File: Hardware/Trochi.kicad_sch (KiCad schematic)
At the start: 37 parts, among them IC1 ICM-42688-P, J1 JST PH, J2 JST-SH, J3 JST-SH, J4 JST-SH, J5 JST-SH, J6 JST_SH, Q1 AO3400A, Q2 AO3400A, Q3 AO3400A, Q4 AO3400A, SW1 SW_SPDT, U1 ME6211C33M5

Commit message: feat: add 3.3V regulator status LED to schematic
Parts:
- added D5: LED_RED, symbol Device:LED_Small_Filled
- added R4: 1K, symbol Device:R_Small_US
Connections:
- net +3.3V: now also D5.2 (A)
- net GND: now also R4.2
- new net: D5.1 (K), R4.1
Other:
- moved on the sheet: D1, D2, D3, D4, J2, J3, J4, J5, J6, Q1, Q2, Q3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

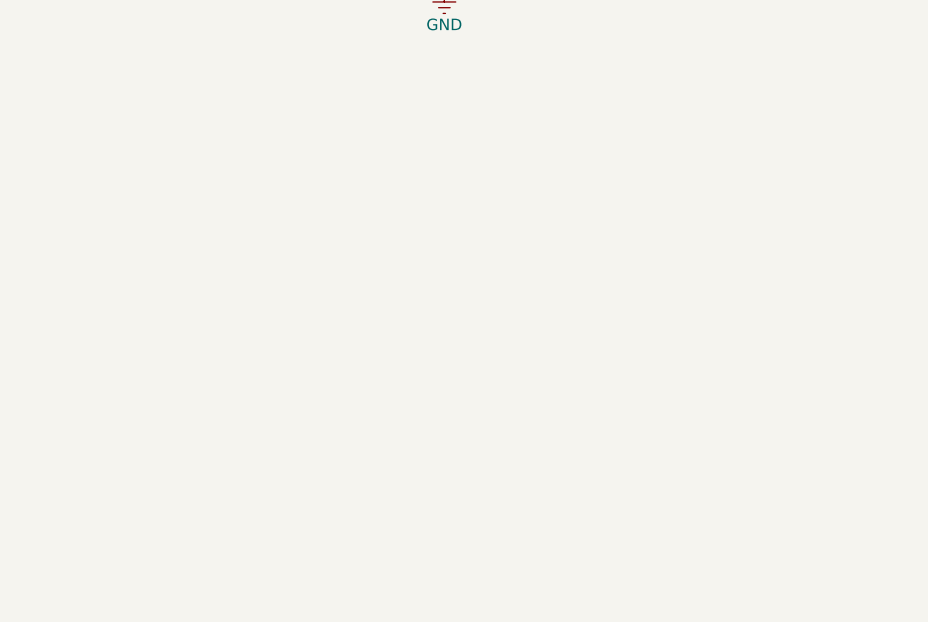
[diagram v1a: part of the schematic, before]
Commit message: feat: add buzzer circuit to schematic
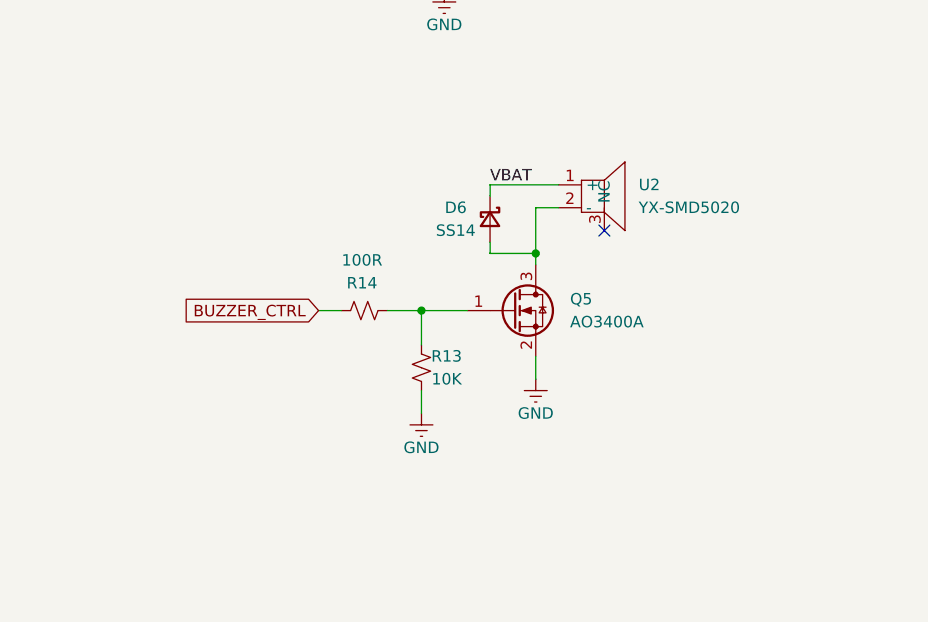
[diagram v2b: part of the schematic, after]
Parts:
- added D6: SS14, symbol Device:D_Schottky_Small
- added Q5: AO3400A, Package_TO_SOT_SMD:SOT-23, symbol Transistor_FET:AO3400A
- added R13: 10K, symbol Device:R_Small_US
- added R14: 100R, symbol Device:R_Small_US
- added U2: YX-SMD5020, trochi_footprint:BUZ-SMD_3P_L5.0-W5.0-P3.50-TL, symbol trochi_sym:YX-SMD5020
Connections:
- net GND: now also Q5.2 (S), R13.2
- net VBAT: now also D6.1 (K), U2.1 (+)
- new net: Q5.1 (G), R13.1, R14.2
- new net: D6.2 (A), Q5.3 (D), U2.2 (-)
- new net BUZZER_CTRL: R14.1
- no-connect marks 4 -> 5

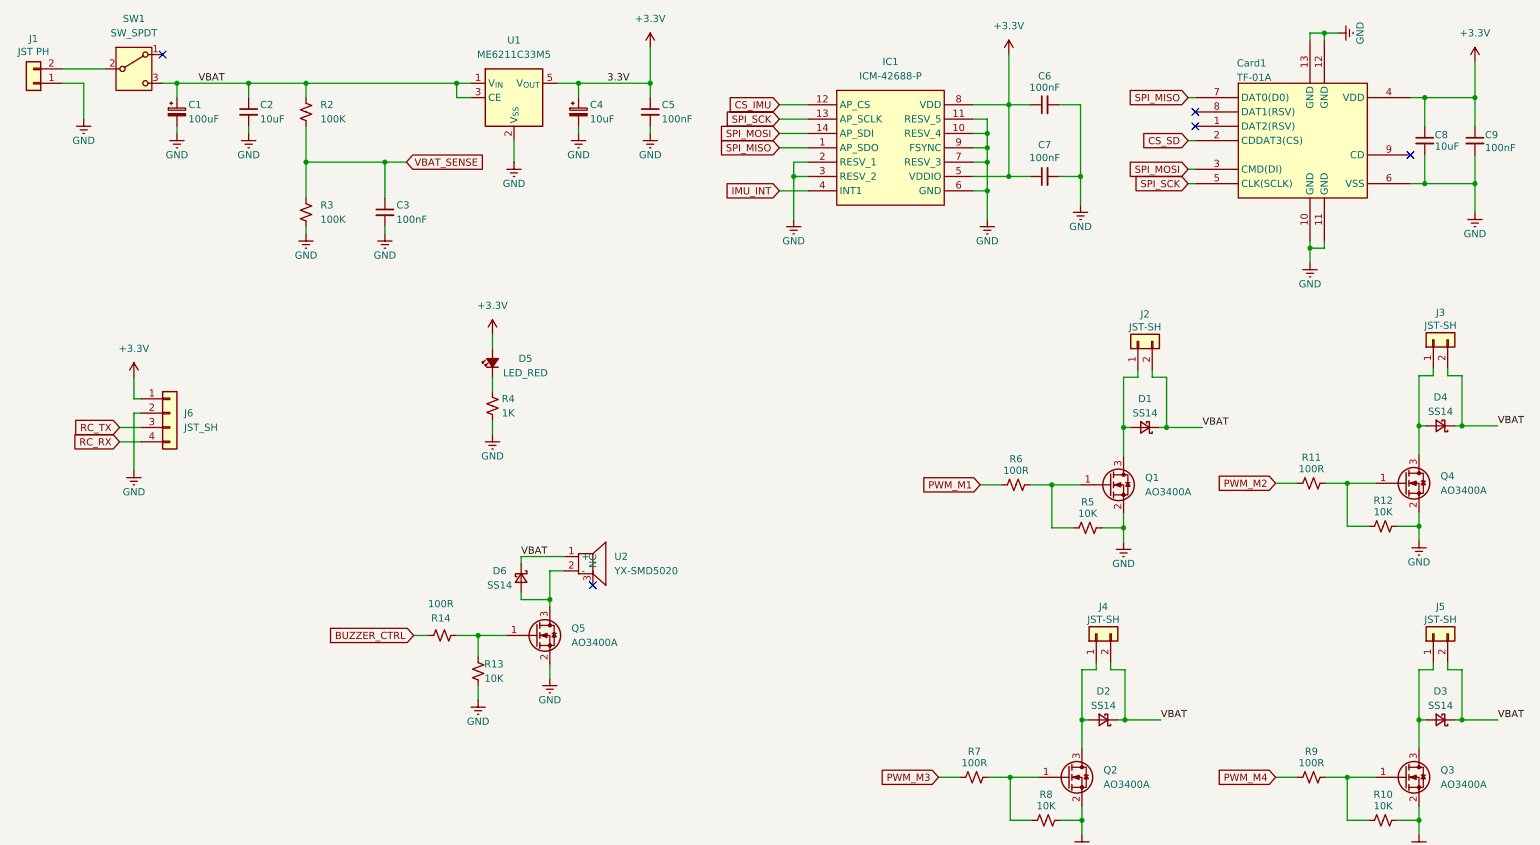
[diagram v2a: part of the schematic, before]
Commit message: feat: add pull-up resistors to SPI bus for IMU and SD card stability
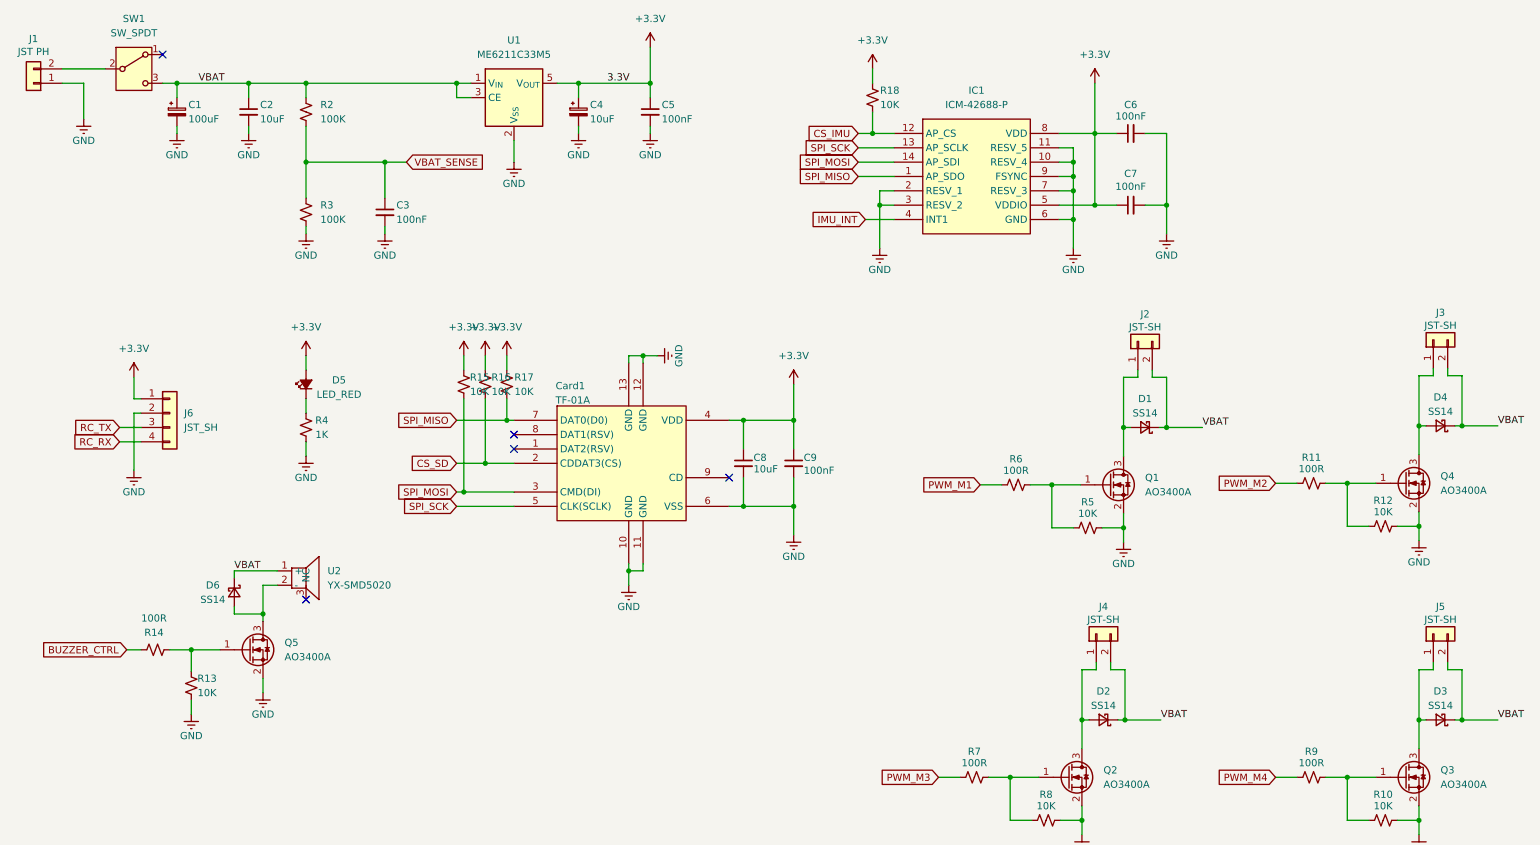
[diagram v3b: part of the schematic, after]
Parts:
- added R15, R16, R17, R18: 10K, symbol Device:R_Small_US
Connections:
- net +3.3V: now also R15.1, R16.1, R17.1, R18.1
- net CS_IMU: now also R18.2
- net CS_SD: now also R16.2
- net SPI_MISO: now also R17.2
- net SPI_MOSI: now also R15.2
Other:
- moved on the sheet: C6, C7, C8, C9, Card1, D5, D6, IC1, Q5, R13, R14, R4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

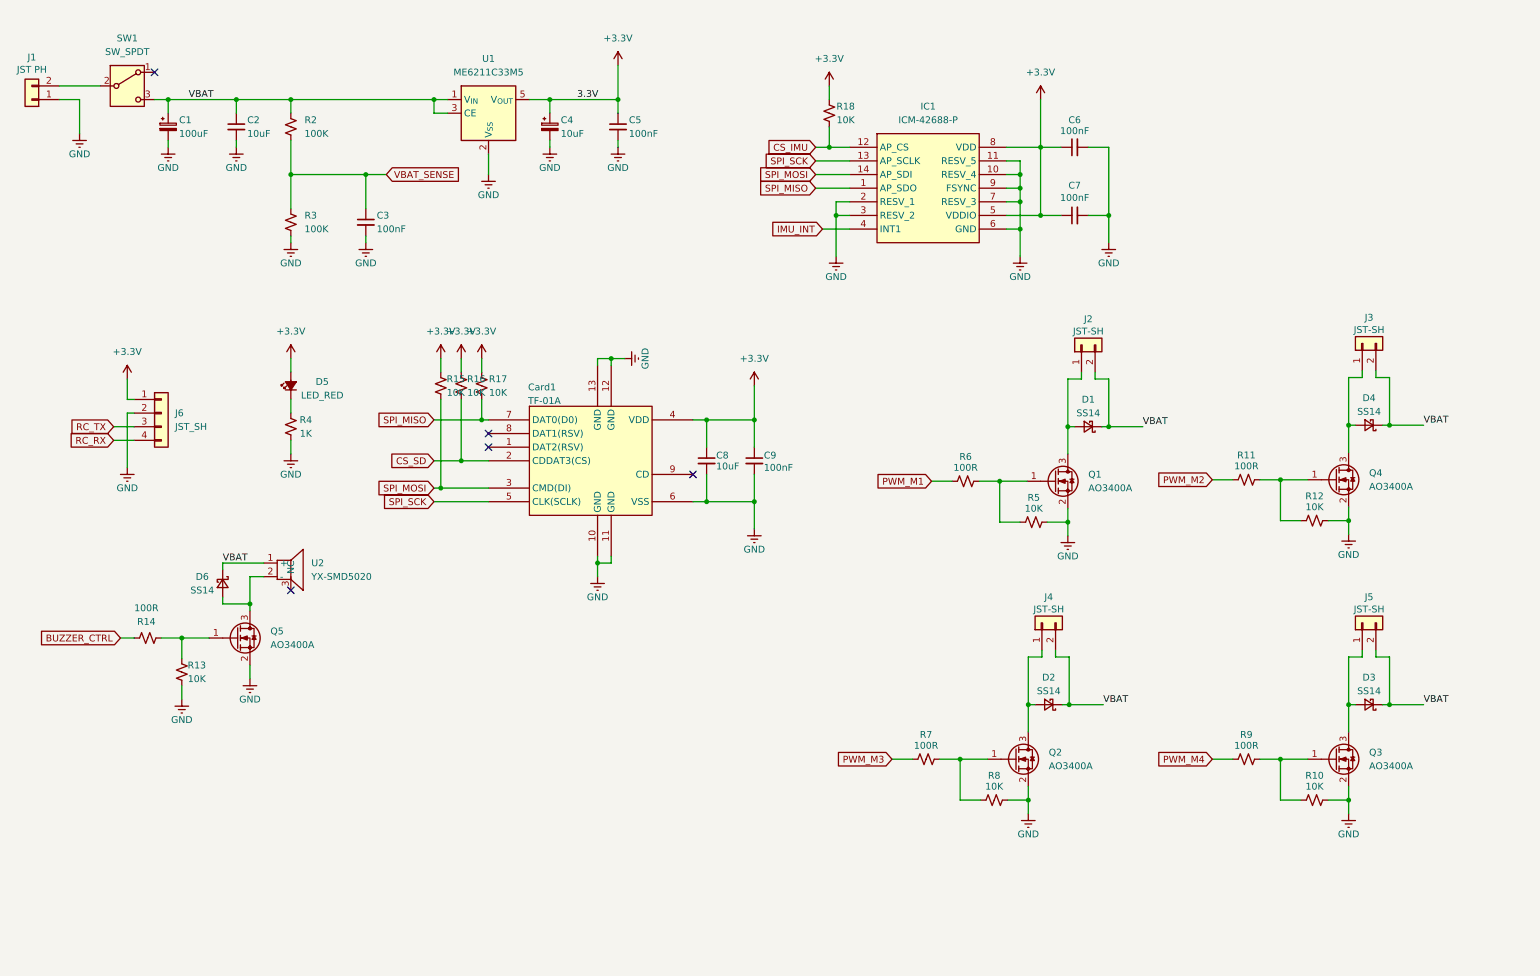
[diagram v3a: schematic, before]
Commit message: feat: add ESP32-S3 SuperMini to schematic with pin assignments
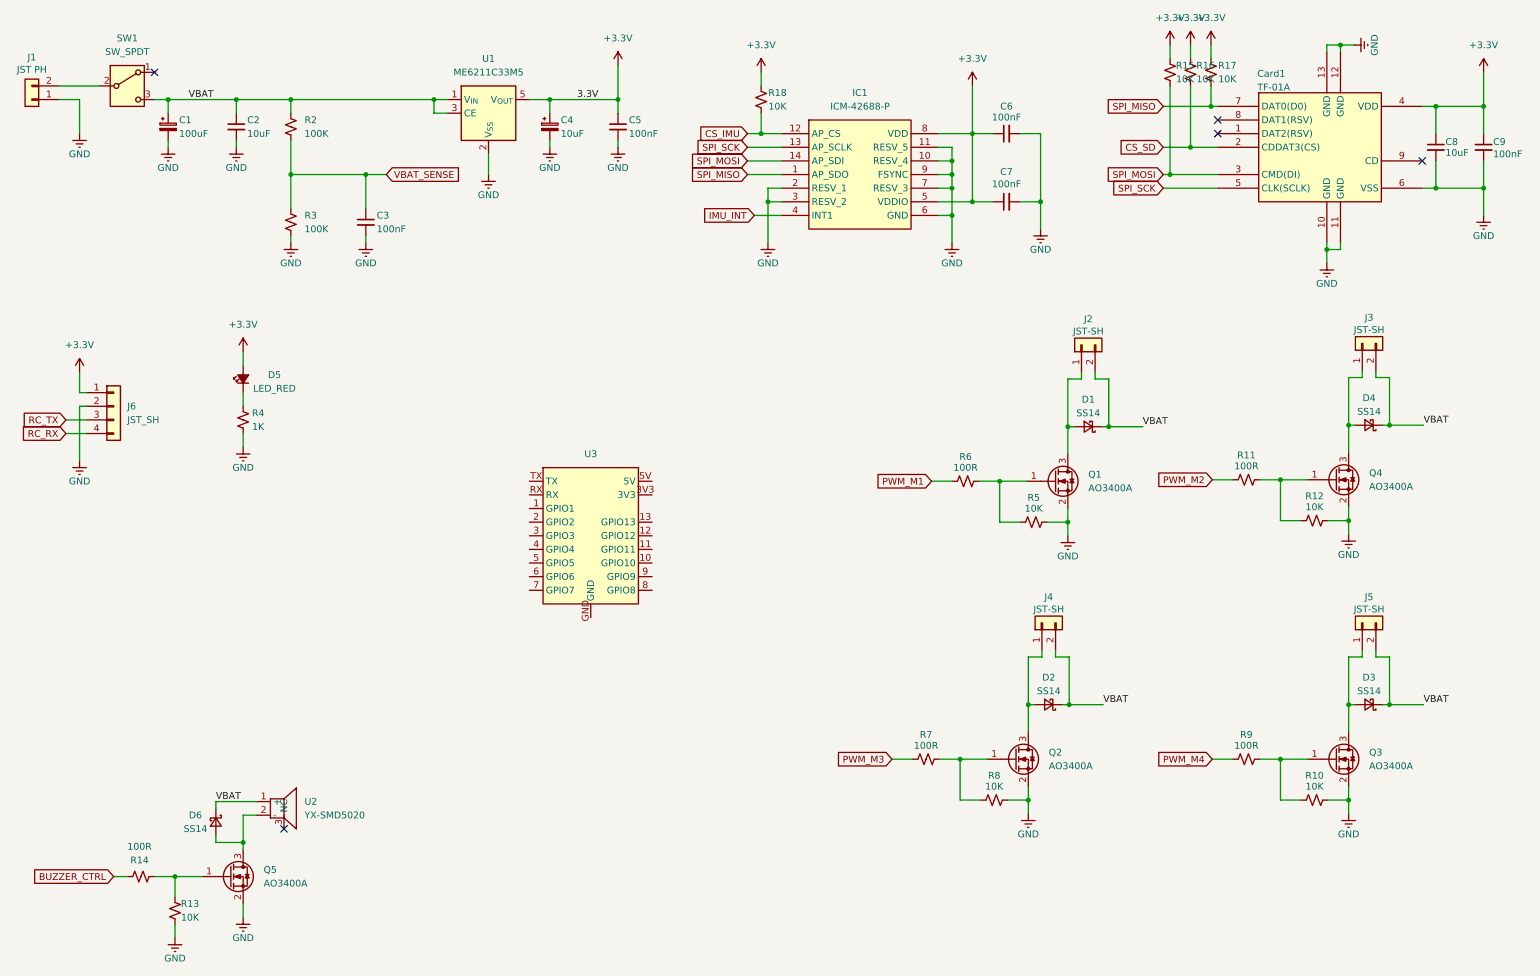
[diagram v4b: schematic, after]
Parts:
- added U3: (no value), trochi_footprint:esp32_s3_supermini, symbol trochi_sym:esp32_s3_supermini
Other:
- moved on the sheet: C6, C7, C8, C9, Card1, D5, D6, IC1, J6, Q5, R13, R14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

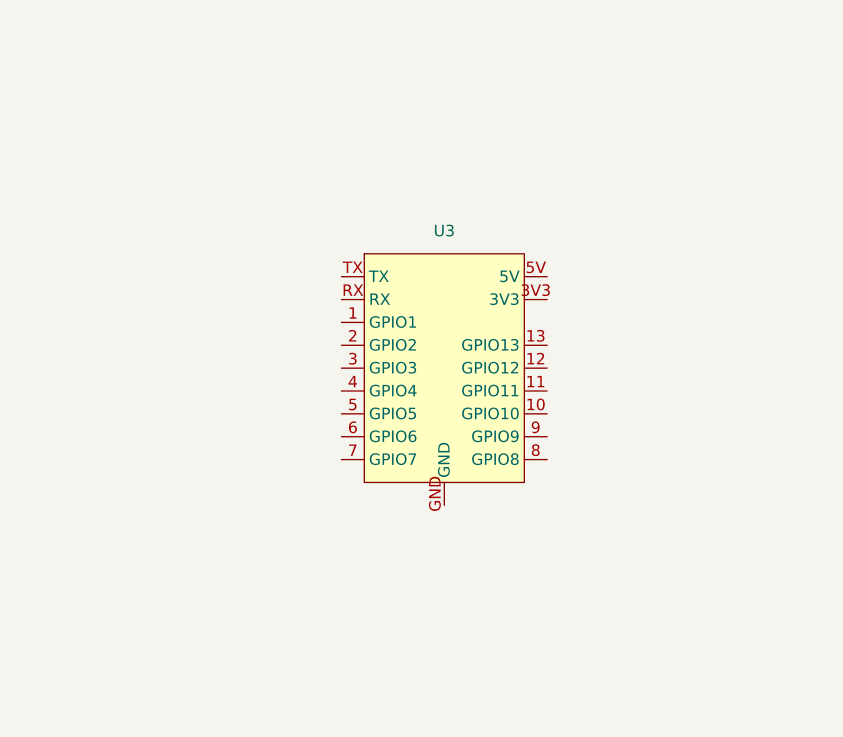
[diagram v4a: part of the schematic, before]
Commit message: feat: wire ESP32-S3 SuperMini header net connections
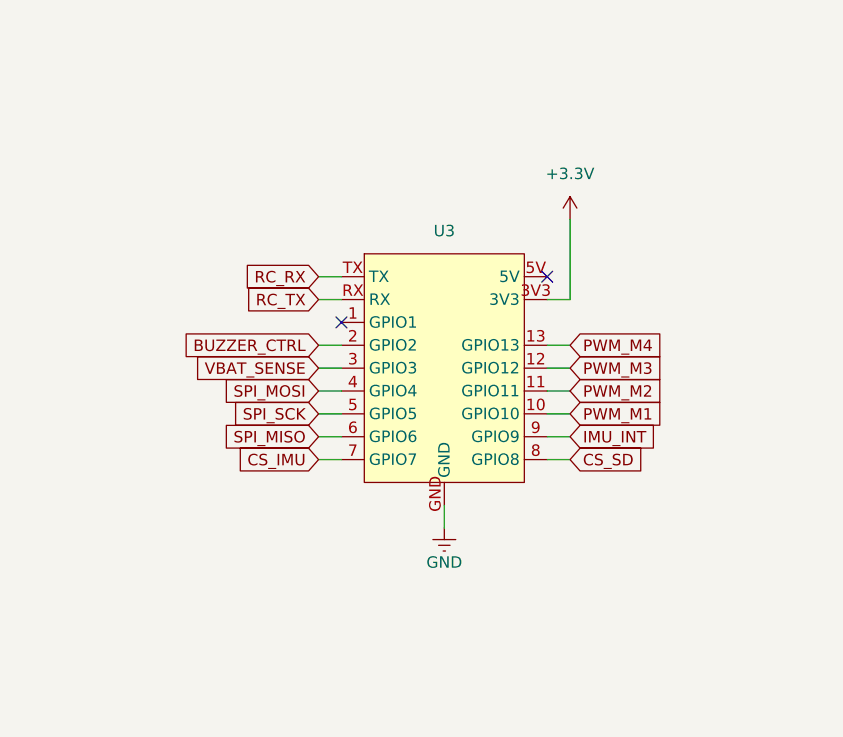
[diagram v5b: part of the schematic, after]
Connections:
- net +3.3V: now also U3.3V3
- net BUZZER_CTRL: now also U3.2 (GPIO2)
- net CS_IMU: now also U3.7 (GPIO7)
- net CS_SD: now also U3.8 (GPIO8)
- net GND: now also U3.GND
- net IMU_INT: now also U3.9 (GPIO9)
- net PWM_M1: now also U3.10 (GPIO10)
- net PWM_M2: now also U3.11 (GPIO11)
- net PWM_M3: now also U3.12 (GPIO12)
- net PWM_M4: now also U3.13 (GPIO13)
- net RC_RX: now also U3.TX
- net RC_TX: now also U3.RX
- net SPI_MISO: now also U3.6 (GPIO6)
- net SPI_MOSI: now also U3.4 (GPIO4)
- net SPI_SCK: now also U3.5 (GPIO5)
- net VBAT_SENSE: now also U3.3 (GPIO3)
- no-connect marks 5 -> 7

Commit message: style: organize and finalize schematic layout
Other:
- note added: "BUZZER"
- note added: "DRIVER'S"
- note added: "EXT"
- note added: "IMU"
- note added: "MCU"
- note added: "POWER"
- note added: "TF-CARD"
- moved on the sheet: C1, C2, C3, C4, C5, C6, C7, C8, C9, Card1, D1, D2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

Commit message: docs: specify schematic title block details
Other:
- company: (none) -> 2j87
- title: (none) -> Trochi
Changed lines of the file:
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@@
 	(generator_version "10.0")
 	(paper "A4")
+	(title_block
+		(title "Trochi")
+		(date "2026-08-29")
+		(rev "V1.0")
+		(company "2j87")
+		(comment 3 "Ankara/Turkey")
+		(comment 4 "Designed by Kerem Bal")
+	)
 	(rectangle
 		(start 11.938 143.51)
